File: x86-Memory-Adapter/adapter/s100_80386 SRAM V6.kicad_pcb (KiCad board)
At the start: 2 copper layers, 254 x 134.6 mm, 71 parts, among them P1 CONN_1, P10 CPLD SPARE, P2 CONN_1, P20 S100_MALE, P3 CONN_1, P34 CONN_1, P35 CONN_1, P4 CONN_1, P5 CONN_20X2, P6 CONN_25X2, P7 XILINX CABLE2, P8 CONN_20X2, P9 CONN_20X2, U1 LDO_REG_7805, U10 74LVX3245, U11 74LVX3245, U12 74LVX3245, U13 74LVX3245, U14 XC9572XL-VQ44, U17 74F04, U2 74LVC573, U3 74LVC573, U4 74LVC573, U5 74LVC573, U6 74LVC573, U7 LM1086CS_TO252_DPAK, U8 74F14, U9 74LVX3245

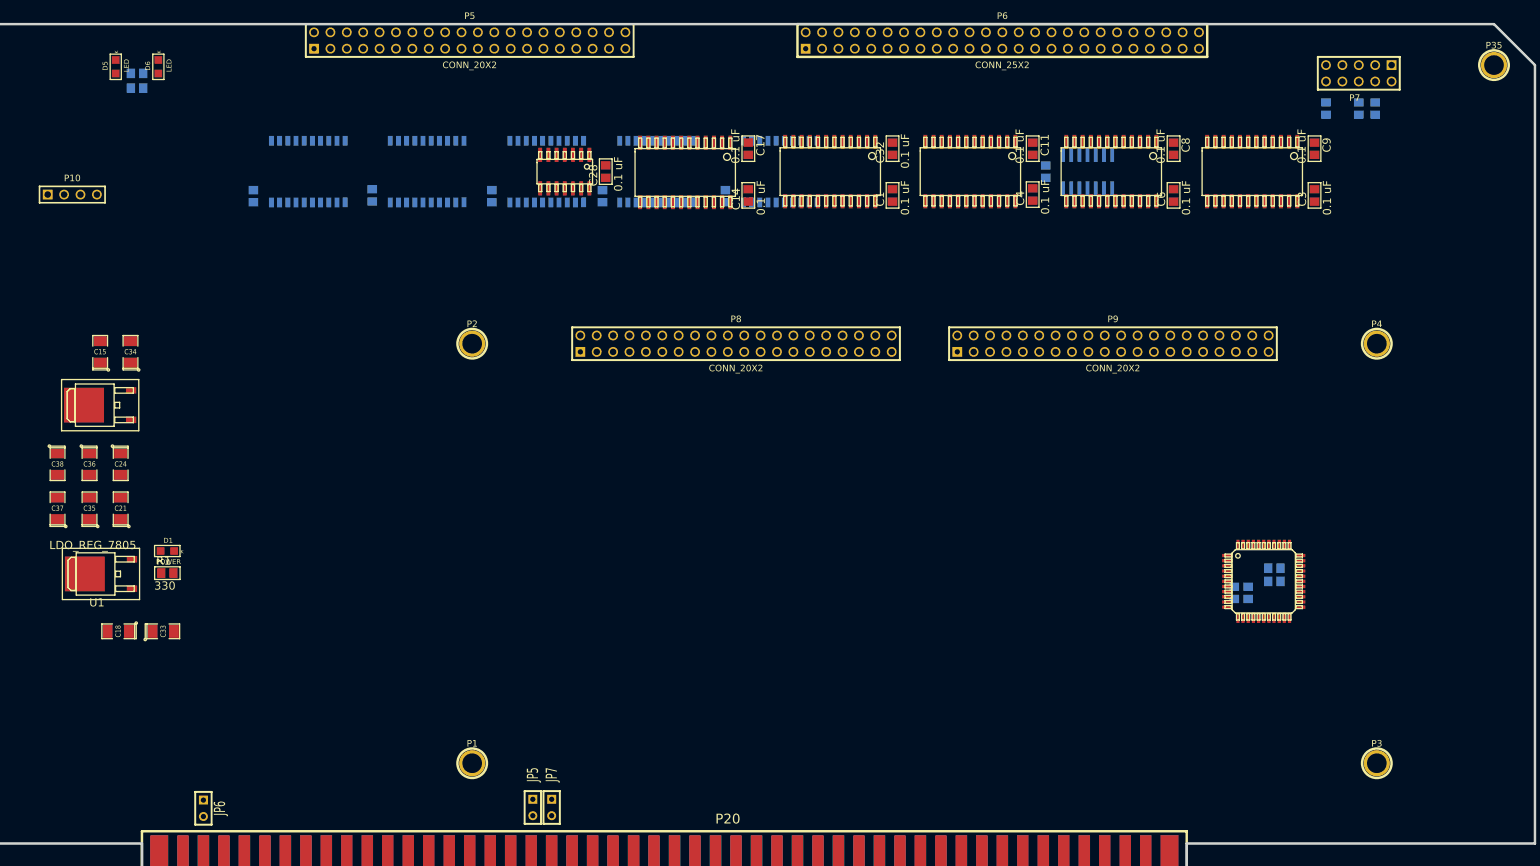
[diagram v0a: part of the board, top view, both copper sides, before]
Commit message: x86-Memory-Adapter: adapter JTAG chain jumper, mezzanine JTAG, CPLD spare header
Source: S100 4GB DRAM BOARD/S100 80386 SRAM DB Version 1/backups/24-04-2015 1921
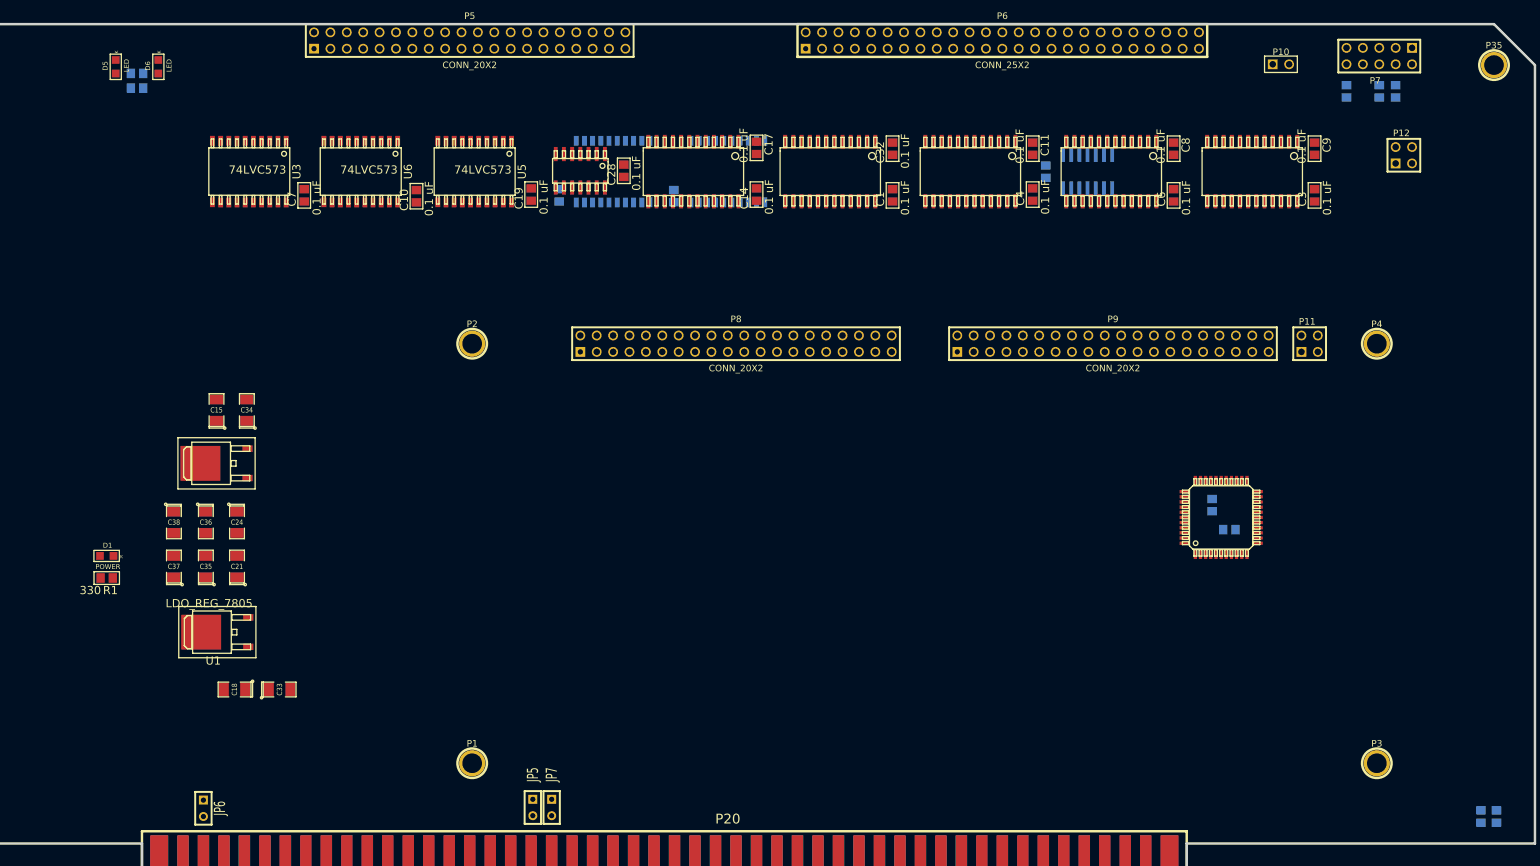
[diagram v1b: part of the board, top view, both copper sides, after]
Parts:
- added P11: CONN_2X2, PIN_ARRAY_2X2, F.Cu at (239.4, 82.5)
- added P12: JTAG CHAIN, PIN_ARRAY_2X2, F.Cu at (254.0, 53.3)
- C10, C19, C7, U3, U5, U6: moved to F.Cu
- P10: value CPLD SPARE -> CPLD Spare; footprint PIN_ARRAY_4x1 -> PIN_ARRAY_2X1
- moved P10 188.4 mm to (234.9, 39.2)
- moved R8 51.6 mm to (268.4, 155.8), turned to 90 degrees
- moved R9 50.0 mm to (265.9, 155.8), turned to 90 degrees
- moved C15 20.2 mm to (70.0, 92.8)
- moved C18 20.2 mm to (72.8, 136.1)
- moved C24 20.2 mm to (73.2, 110.2)
- moved C33 20.2 mm to (79.8, 136.1)
- moved C34 20.2 mm to (74.7, 92.8)
- moved C38 20.2 mm to (63.4, 110.2)
- moved U1 20.2 mm to (70.1, 127.3)
- moved U7 20.2 mm to (70.0, 101.1)
- moved C36 20.2 mm to (68.3, 110.2)
- moved C21 20.2 mm to (73.2, 117.1)
- moved C37 20.2 mm to (63.4, 117.1)
- moved C35 20.2 mm to (68.3, 117.1)
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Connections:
- P10 pad 1: /CPLD_P7 -> /CPLD_P23
- P10 pad 2: /CPLD_P8 -> /CPLD_P44
- P7 pad 8: /CPLD1_TDO -> /TDO_1
- P9 pad 29: (no net) -> /CPLD_P2
- P9 pad 31: /CPLD_P2 -> /CPLD_P3
- P9 pad 33: /CPLD_P3 -> /CPLD_P5
- P9 pad 35: /CPLD_P5 -> /CPLD_P6
- P9 pad 37: /CPLD_P6 -> /CPLD_P7
- P9 pad 38: (no net) -> /CPLD_P8
- R8 pad 1: /V3.3 -> (no net)
- R8 pad 2: N-00000119 -> (no net)
- R9 pad 1: /V3.3 -> (no net)
- R9 pad 2: N-0000017 -> (no net)
- U14 pad 15: (no net) -> /V3.3
- U14 pad 26: N-0000017 -> /V3.3
- U14 pad 35: N-00000119 -> /V3.3
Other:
- net class Default: via_dia 0.889 -> 0.6; via_drill 0.5588 -> 0.425
- net class Power 8v: trace_width 2 -> 1.6
- net class gnd added: clearance 0.1905, trace_width 0.45, via_dia 0.889, via_drill 0.5588
- rule via_min_drill: 0.508 -> 0.35
- rule via_min_size: 0.889 -> 0.5

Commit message: x86-Memory-Adapter: adapter LT3081 adjustable rail and 3.3V/5V source jumpers; first routing
Source: S100 4GB DRAM BOARD/S100 80386 SRAM DB Version 1/backups/25-04-2015 1211
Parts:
- moved U8 81.3 mm to (186.9, 110.0), turned to 90 degrees
- moved C28 81.2 mm to (186.9, 116.6), turned to 0 degrees
- moved U17 14.6 mm to (212.1, 68.6)
- moved C22 14.4 mm to (205.2, 68.6)
- moved C26 9.78 mm to (113.3, 59.4)
- moved U2 9.78 mm to (121.7, 55.9)
- moved U11 7.75 mm to (136.1, 55.9)
- moved C14 7.12 mm to (146.6, 59.7)
- moved C17 7.11 mm to (146.6, 52.1)
- moved U9 4.32 mm to (234.8, 55.9)
- moved C3 4.32 mm to (244.5, 59.6)
- moved C9 4.32 mm to (244.5, 52.3)
- moved C6 3.05 mm to (221.4, 59.6)
- moved C8 3.05 mm to (221.4, 52.3)
- moved U12 3.05 mm to (211.7, 55.9)
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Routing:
- net GND: track 0.00 -> 1185.8 mm, vias 0 -> 16
- net /V3.3: track 0.00 -> 492.4 mm, vias 0 -> 4
- net VCC: track 0.00 -> 355.0 mm, vias 0 -> 6
- net /CPLD_P33: track 0.00 -> 198.3 mm, vias 0 -> 2
- net /CPLD_P31: track 0.00 -> 197.0 mm, vias 0 -> 2
- net /CPLD_P39: track 0.00 -> 193.4 mm, vias 0 -> 5
- net /DB_ADS: track 0.00 -> 191.1 mm, vias 0 -> 4
- net /CPLD_P41: track 0.00 -> 180.9 mm, vias 0 -> 2
- net /CPLD_P21: track 0.00 -> 177.3 mm
- net /CPLD_P22: track 0.00 -> 175.9 mm
- net /CPLD_P43: track 0.00 -> 173.4 mm, vias 0 -> 2
- net /CPLD_P14: track 0.00 -> 170.9 mm, vias 0 -> 2
- net /CPLD_P42: track 0.00 -> 169.5 mm, vias 0 -> 2
- net /CPLD_P16: track 0.00 -> 169.5 mm, vias 0 -> 3
- net /CPLD_P18: track 0.00 -> 169.4 mm, vias 0 -> 3
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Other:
- net class Default: clearance 0.1905 -> 0.22; trace_width 0.21 -> 0.25
- net class Power: clearance 0.1905 -> 0.22
- net class Power 8v: clearance 0.2 -> 0.22
- net class gnd: trace_width 0.45 -> 0.35
- rule trace_clearance: 0.1905 -> 0.22

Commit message: x86-Memory-Adapter: adapter power section simplified; routed board and gerbers
Source: S100 4GB DRAM BOARD/S100 80386 SRAM DB Version 1/backups/20-06-2015 1159 - need to move CPLD
The folder was made on 20-06-2015 but its files were last saved on 25-04-2015 (gerbers 14:47), so the commit carries the April date.
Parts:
- removed R8, R9: 3v, ^^SMD_Resistor-0805
- added C12: 10 uF, SM1206_Opendous, F.Cu at (45.9, 129.0)
- added C16: 10 uF, SM1206_Opendous, F.Cu at (49.1, 129.0)
- added C20: 10 uF, SM1206_Opendous, F.Cu at (42.6, 129.0)
- added C23: 10 uF, SM1206_Opendous, F.Cu at (47.4, 146.2)
- added C25: 10 uF, SM1206_Opendous, F.Cu at (43.0, 146.2)
- added K1: 3.3V, SIL-3, F.Cu at (51.2, 91.8)
- added K2: 5V, SIL-3, F.Cu at (51.2, 98.6)
- added P13: LT Output select, PIN_ARRAY_6X2, F.Cu at (38.7, 114.3)
- added R10: 500, ^^SMD_Resistor-0805, F.Cu at (35.2, 146.2)
- added R11: 24.3K, ^^SMD_Resistor-0805, F.Cu at (33.3, 120.9)
- added R12: 36.5K, ^^SMD_Resistor-0805, F.Cu at (33.3, 115.6)
- added R13: 66.5K, ^^SMD_Resistor-0805, F.Cu at (33.3, 110.5)
- added R14: 1K, ^^SMD_Resistor-0805, F.Cu at (38.2, 146.2)
- added R15: 30.1K, ^^SMD_Resistor-0805, F.Cu at (33.3, 118.1)
- added R16: 49.9K, ^^SMD_Resistor-0805, F.Cu at (33.3, 113.0)
- added R17: 100K, ^^SMD_Resistor-0805, F.Cu at (33.3, 108.0)
- added R18: 300, ^^SMD_Resistor-0805, F.Cu at (56.4, 129.4)
- added R7: 4.53k, ^^SMD_Resistor-0805, F.Cu at (38.6, 129.3)
- added U20: LT3081, ^^LT3081_TSSOP16, F.Cu at (41.9, 137.6)
- moved D1 9.21 mm to (59.5, 122.0)
- moved R1 8.86 mm to (59.4, 124.9)
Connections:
- C21 pad 1: VCC -> /LM7805 out
- C24 pad 1: /V3.3 -> /LM1086 out
- C35 pad 1: VCC -> /LM7805 out
- C36 pad 1: /V3.3 -> /LM1086 out
- C37 pad 1: VCC -> /LM7805 out
- C38 pad 1: /V3.3 -> /LM1086 out
- U1 pad 3: VCC -> /LM7805 out
- U7 pad 3: /V3.3 -> /LM1086 out
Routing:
- net GND: track 1185.8 -> 1601.9 mm, vias 16 -> 62
- net /LTout: track 0.00 -> 84.8 mm
- net /LM7805 out: track 0.00 -> 42.9 mm
- net /LM1086 out: track 0.00 -> 35.2 mm
- net /+8Vi: track 161.2 -> 193.8 mm
- net /V3.3: track 492.4 -> 459.8 mm
- net N-00000131: track 0.00 -> 31.4 mm
- net VCC: track 355.0 -> 376.7 mm, vias 6 -> 5
- net N-00000119: track 0.00 -> 9.06 mm
- net N-00000118: track 0.00 -> 6.58 mm
- net N-00000120: track 0.00 -> 5.90 mm
- net N-00000108: track 6.94 -> 2.99 mm
- net N-00000132: track 0.00 -> 3.35 mm
- net N-00000130: track 0.00 -> 3.24 mm
- net N-00000128: track 0.00 -> 3.24 mm
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- added copper zone on F.Cu, net /+8Vi
- added copper zone on F.Cu, net /LTout
- added copper zone on B.Cu, net GND
- added copper zone on F.Cu, net GND
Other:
- outline, holes or cut-outs redrawn
- board text added: "2 4 1 3"
- board text added: "2-4 CPLD only 1-2 & 3-4 CPLD + FPGA"
- board text added: "3.3V"
- board text added: "5.0V"
- board text added: "5.0V 3.3V 2.5V 1.8V 1.5V 1.2V"
- board text added: "<- in LM7805 -> out 5.0V <- in LT3081"
- board text added: "<- in LT3081 -> out 3.3V <- in LM1086"
- board text added: "CPLD Pins"
- board text added: "JTAG Chain"
- board text added: "LT3081 Output Voltage Selector"
- board text added: "P23 P44"
- board text added: "POWER"
- board text added: "U10"
- board text added: "U11"
- board text added: "U12"
- board text added: "U13"
- board text added: "U14"
- board text added: "U20"
- board text added: "U7"
- board text added: "U8"
- board text added: "U9"
- board text added: "XC9572XL"
- board text added: "XILINX CABLE"
- board text added: "x86 32bit Memory Adapter Board Rev 1.0"
- board text added: "x86 32bit Memory Adapter Board © 2015 A Burrows R1.0 2715"
- board text removed: "S-100 80386 SRAM BOARD VERSION 06"

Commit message: x86-Memory-Adapter: adapter CPLD moved to bottom; add general I/O, 23LC1024, select LED
Source: S100 4GB DRAM BOARD/S100 80386 SRAM DB Version 1/backups/21-06-2015 1724
Board partly re-routed after the move. The April gerbers are kept.
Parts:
- added C2: 0.1 uF, ^^SMD_Resistor-0805, F.Cu at (56.0, 78.4)
- added D2: LED, ^^LED-0805, F.Cu at (237.6, 35.9)
- added P14: GenIO_1, PIN_ARRAY_6X2, F.Cu at (242.2, 125.0)
- added P15: GenIO_2, PIN_ARRAY_6X2, F.Cu at (51.3, 41.9)
- added R19: 10k, ^^SMD_Resistor-0805, B.Cu at (56.0, 72.6)
- added R20: 1K, ^^SMD_Resistor-0805, B.Cu at (46.6, 71.5)
- added R21: 10K, ^^SMD_Resistor-0805, B.Cu at (65.5, 64.3)
- added R22: 10K, ^^SMD_Resistor-0805, B.Cu at (65.5, 67.4)
- added R23: 10K, ^^SMD_Resistor-0805, B.Cu at (65.5, 70.1)
- added R8: 330, ^^SMD_Resistor-0805, B.Cu at (239.0, 37.0)
- added R9: 10K, ^^SMD_Resistor-0805, B.Cu at (56.0, 64.9)
- added U15: ZZZZ1, ^^ZZZZZZ1, F.Cu at (179.7, 137.8)
- added U16: ^^74LV244, ^^SO-20wide, F.Cu at (56.0, 69.3)
- added U18: 23LC1024, DIP-8__300_ELL, F.Cu at (39.2, 71.6)
- C1, C28, C3, C32, C9, U13, U14, U8, U9: moved to B.Cu
- C22, C27, C30, U17: moved to F.Cu
- moved R5 178.2 mm to (235.7, 37.0), turned to 90 degrees
- moved D5 176.9 mm to (231.3, 35.9)
- moved R6 174.9 mm to (232.5, 37.0), turned to 90 degrees
- moved D6 173.5 mm to (234.4, 35.9)
- moved C28 87.0 mm to (267.0, 82.6), turned to 270 degrees
- moved U8 78.5 mm to (260.5, 82.6), turned to 180 degrees
- moved P10 72.3 mm to (263.4, 105.7)
- moved U17 48.3 mm to (260.4, 67.6)
- moved C22 48.3 mm to (253.5, 67.6), turned to 270 degrees
- moved C27 23.3 mm to (246.3, 99.9)
- moved C3 22.2 mm to (222.7, 55.3)
- moved C9 22.2 mm to (222.7, 48.1)
- moved U14 20.7 mm to (244.9, 101.8)
- moved C30 18.3 mm to (243.6, 103.7), turned to 0 degrees
- moved C1 14.4 mm to (161.5, 55.2)
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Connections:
- U14 pad 32: (no net) -> /BOARD_SELECT
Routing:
- net GND: track 1601.9 -> 249.2 mm, vias 62 -> 7
- net /V3.3: track 459.8 -> 0.00 mm, vias 4 -> 0
- net VCC: track 376.7 -> 1.84 mm, vias 5 -> 1
- net /CPLD_P33: track 198.3 -> 0.00 mm, vias 2 -> 0
- net /CPLD_P31: track 197.0 -> 0.00 mm, vias 2 -> 0
- net /CPLD_P39: track 193.4 -> 0.00 mm, vias 5 -> 0
- net /DB_ADS: track 190.1 -> 0.00 mm, vias 4 -> 0
- net /CPLD_P41: track 180.9 -> 0.00 mm, vias 2 -> 0
- net /CPLD_P21: track 177.3 -> 0.00 mm
- net /CPLD_P22: track 175.9 -> 0.00 mm
- net /CPLD_P43: track 173.4 -> 0.00 mm, vias 2 -> 0
- net /CPLD_P14: track 170.9 -> 0.00 mm, vias 2 -> 0
- net /CPLD_P42: track 169.5 -> 0.00 mm, vias 2 -> 0
- net /CPLD_P16: track 169.5 -> 0.00 mm, vias 3 -> 0
- net /CPLD_P18: track 169.4 -> 0.00 mm, vias 3 -> 0
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- removed copper zone on B.Cu, net GND
- removed copper zone on F.Cu, net GND

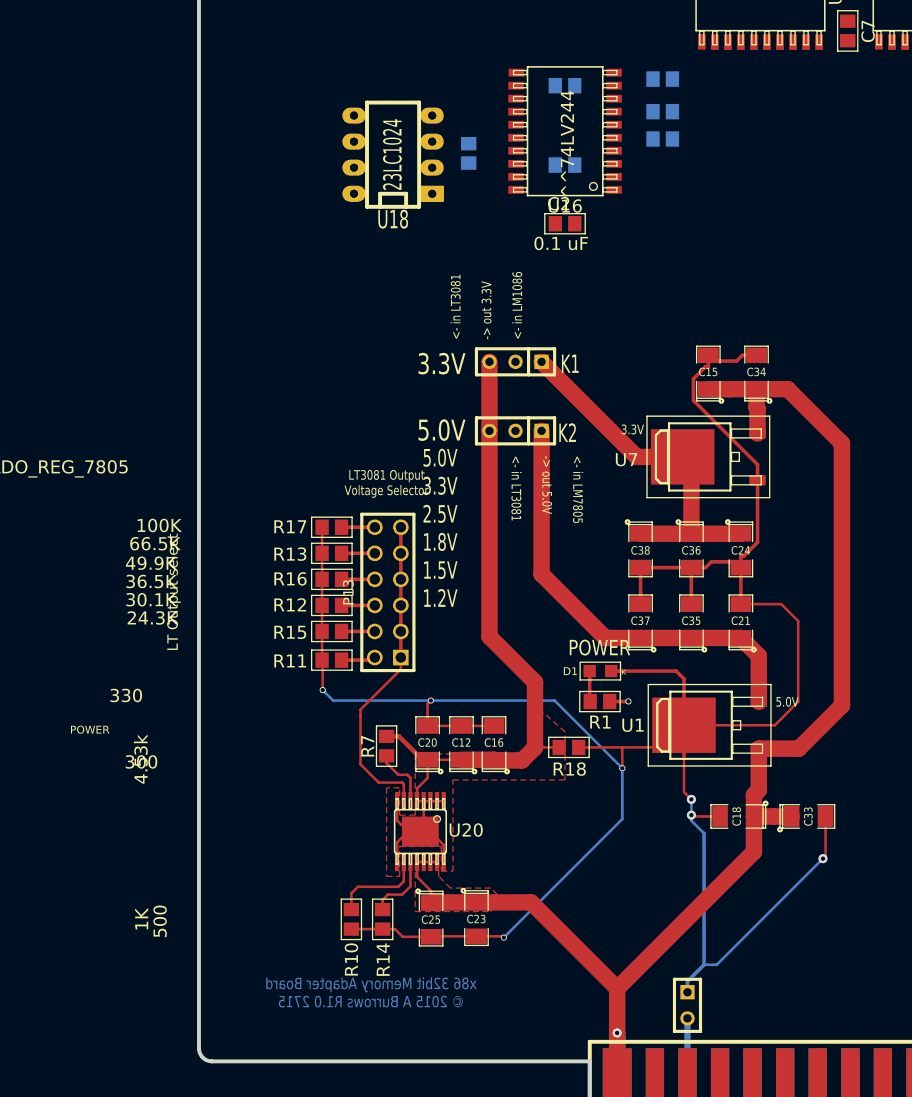
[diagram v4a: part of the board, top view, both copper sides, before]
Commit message: x86-Memory-Adapter: adapter LM2596 buck pre-regulator for the LT3081
Source: S100 4GB DRAM BOARD/S100 80386 SRAM DB Version 1/backups/17-07-2015 2113
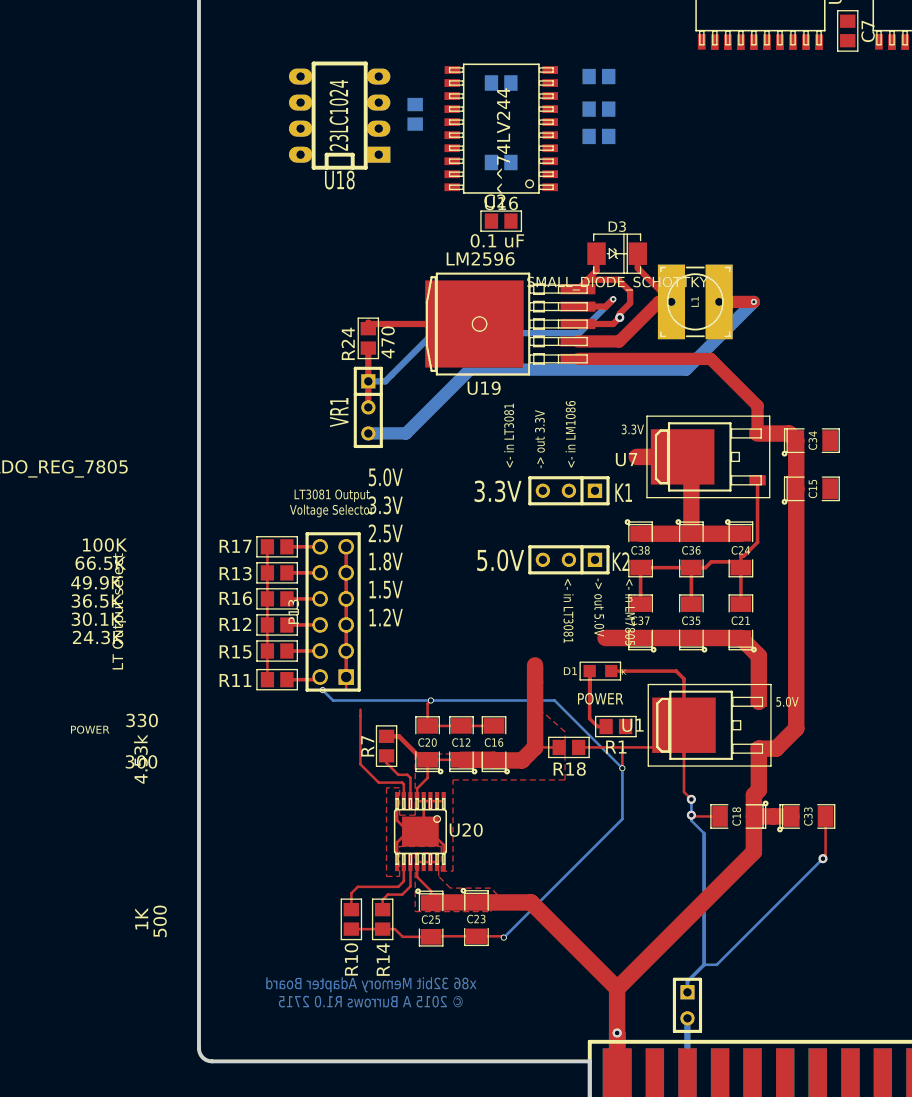
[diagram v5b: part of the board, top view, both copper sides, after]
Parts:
- added D3: SMALL_DIODE_SCHOTTKY, DO-214AA(SMB), F.Cu at (61.1, 81.3)
- added L1: SMALL_INDUCTANCE, Inductor_CDRH6D28, F.Cu at (68.7, 86.0)
- added R24: 470, ^^SMD_Resistor-0805, F.Cu at (36.8, 89.5)
- added U19: LM2596, ^^TO263-51, F.Cu at (50.7, 88.1)
- added VR1: VR1, ^^Variable_Resistor, F.Cu at (36.8, 96.3)
- moved C15 15.3 mm to (80.2, 104.2), turned to 0 degrees
- moved K1 13.6 mm to (56.4, 104.4)
- moved K2 13.6 mm to (56.4, 111.1)
- moved C34 8.66 mm to (80.2, 99.5), turned to 0 degrees
- moved R20 6.45 mm to (41.4, 67.7)
- moved U18 6.45 mm to (34.0, 67.8)
- moved C2 6.23 mm to (49.8, 78.1)
- moved R19 6.23 mm to (49.8, 72.4)
- moved R21 6.23 mm to (59.3, 64.0)
- moved R22 6.23 mm to (59.3, 67.2)
- moved R23 6.23 mm to (59.3, 69.8)
- moved R9 6.23 mm to (49.8, 64.6)
- moved U16 6.23 mm to (49.8, 69.1)
- moved R11 5.66 mm to (27.9, 122.8)
- moved R12 5.66 mm to (27.9, 117.5)
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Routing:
- net /LM2596output: track 0.00 -> 46.3 mm, vias 0 -> 1
- net N-00000161: track 0.00 -> 36.7 mm, vias 0 -> 1
- net /LTout: track 84.8 -> 53.4 mm
- net /LM7805 out: track 42.9 -> 20.2 mm
- net GND: track 249.2 -> 226.7 mm, vias 7 -> 8
- net N-00000163: track 0.00 -> 16.8 mm
- net /LM1086 out: track 35.2 -> 22.1 mm
- net N-0000079: track 2.99 -> 9.48 mm
- net N-00000172: track 31.4 -> 25.8 mm
- net /+8Vi: track 136.1 -> 139.8 mm
- net VCC: track 1.84 -> 0.00 mm, vias 1 -> 0
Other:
- net class Default: clearance 0.22 -> 0.25; trace_width 0.25 -> 0.28; via_dia 0.6 -> 0.725; via_drill 0.425 -> 0.5
- rule trace_clearance: 0.22 -> 0.25

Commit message: x86-Memory-Adapter: adapter general I/O and SPI SRAM removed; board re-routed
Source: S100 4GB DRAM BOARD/S100 80386 SRAM DB Version 1 (working folder)
No gerbers were made from this final layout; GERBERS/ is the April 2015 plot.
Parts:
- removed C2: 0.1 uF, ^^SMD_Resistor-0805
- removed P14: GenIO_1, PIN_ARRAY_6X2
- removed P15: GenIO_2, PIN_ARRAY_6X2
- removed R19: 10k, ^^SMD_Resistor-0805
- removed R20: 1K, ^^SMD_Resistor-0805
- removed R21, R22, R23, R9: 10K, ^^SMD_Resistor-0805
- removed U16: ^^74LV244, ^^SO-20wide
- removed U18: 23LC1024, DIP-8__300_ELL
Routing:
- net GND: track 226.7 -> 1205.1 mm, vias 8 -> 19
- net /DB_ADS: track 0.00 -> 368.8 mm, vias 0 -> 7
- net /V3.3: track 0.00 -> 356.2 mm, vias 0 -> 11
- net VCC: track 0.00 -> 331.3 mm, vias 0 -> 6
- net /CPLD_P39: track 0.00 -> 212.8 mm, vias 0 -> 4
- net /CPLD_P41: track 0.00 -> 210.3 mm, vias 0 -> 2
- net /CPLD_P42: track 0.00 -> 202.9 mm, vias 0 -> 3
- net /CPLD_P36: track 0.00 -> 200.6 mm, vias 0 -> 4
- net /CPLD_P40: track 0.00 -> 187.0 mm, vias 0 -> 3
- net /CPLD_P43: track 0.00 -> 177.4 mm, vias 0 -> 4
- net /CPLD_P22: track 0.00 -> 174.5 mm
- net /CPLD_P21: track 0.00 -> 173.7 mm
- net /CPLD_P20: track 0.00 -> 168.8 mm
- net /CPLD_P19: track 0.00 -> 167.5 mm
- net /CPLD_P13: track 0.00 -> 166.5 mm
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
